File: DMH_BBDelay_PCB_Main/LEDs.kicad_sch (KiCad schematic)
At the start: 19 parts, among them Q15 BC548, Q16 BC548, Q17 BC548, Q18 BC548, SW2 SW_DPDT_x2, U19 4020, U20 4020

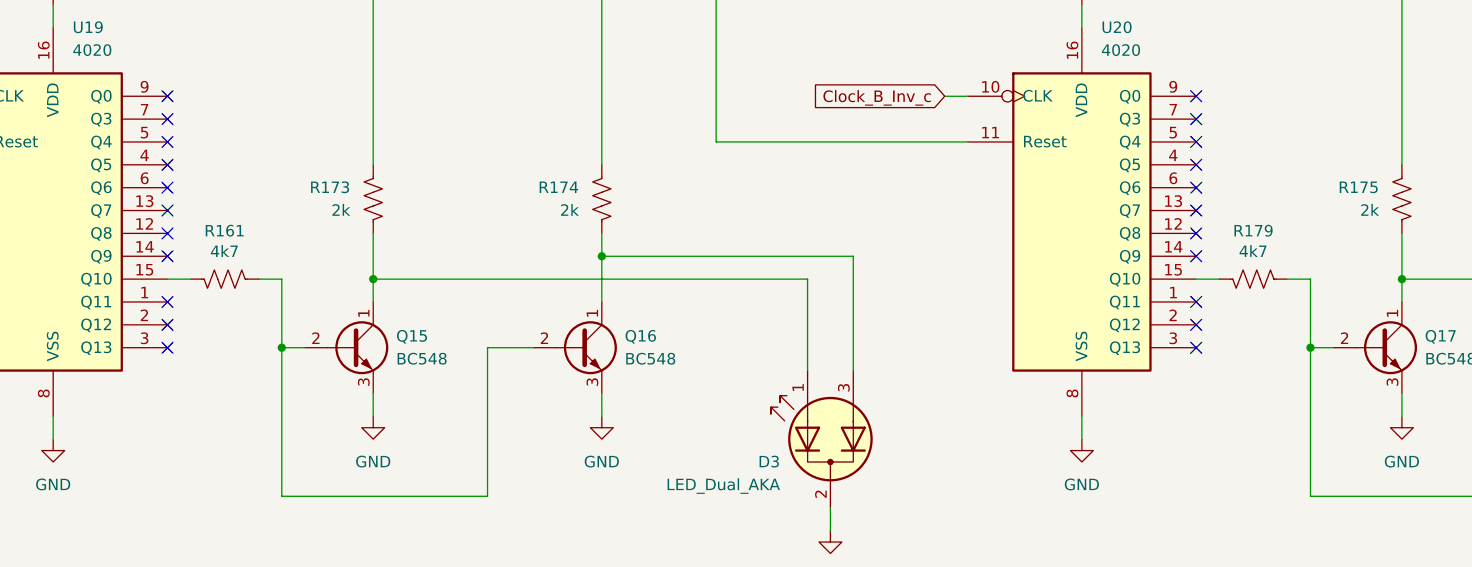
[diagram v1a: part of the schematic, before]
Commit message: Perfected circuit with double V3205
Next step is try quad V3205 per channel to reduce aliasing further
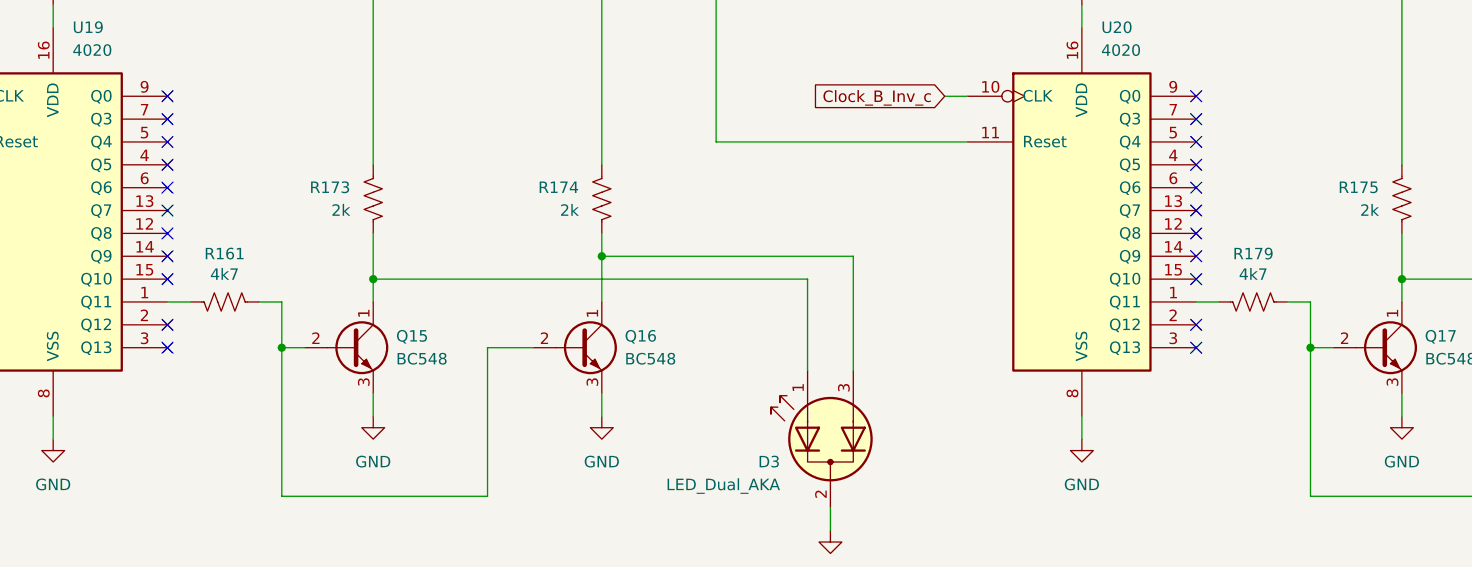
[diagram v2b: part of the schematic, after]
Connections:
- net at U19.1 (Q11): now also R161.1
- net at U19.15 (Q10): no longer R161.1
- net at R179.1: now also U20.1 (Q11); no longer U20.15 (Q10)
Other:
- moved on the sheet: R161, R179
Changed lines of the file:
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@@
 	)
 	(no_connect
-		(at 66.04 91.44)
+		(at 180.34 109.22)
 	)
 	(no_connect
-		(at 66.04 116.84)
+		(at 66.04 91.44)
 	)
 	(no_connect
-		(at 180.34 111.76)
+		(at 66.04 116.84)
 	)
 	(no_connect
@@
 	)
 	(no_connect
+		(at 66.04 109.22)
+	)
+	(no_connect
 		(at 180.34 106.68)
 	)
@@
 	)
 	(no_connect
-		(at 66.04 111.76)
-	)
-	(no_connect
 		(at 180.34 116.84)
 	)
@@
 	(wire
 		(pts
-			(xy 66.04 109.22) (xy 68.58 109.22)
+			(xy 127 69.85) (xy 38.1 69.85)
 		)
 		(stroke
@@
 	(wire
 		(pts
-			(xy 127 69.85) (xy 38.1 69.85)
+			(xy 78.74 111.76) (xy 76.2 111.76)
 		)
 		(stroke
@@
 	(wire
 		(pts
-			(xy 78.74 109.22) (xy 76.2 109.22)
+			(xy 114.3 66.04) (xy 142.24 66.04)
 		)
 		(stroke
@@
 	(wire
 		(pts
-			(xy 114.3 66.04) (xy 142.24 66.04)
+			(xy 180.34 111.76) (xy 182.88 111.76)
 		)
 		(stroke
@@
 	(wire
 		(pts
-			(xy 190.5 109.22) (xy 193.04 109.22)
+			(xy 190.5 111.76) (xy 193.04 111.76)
 		)
 		(stroke
@@
 	(wire
 		(pts
-			(xy 78.74 109.22) (xy 78.74 116.84)
+			(xy 78.74 111.76) (xy 78.74 116.84)
 		)
 		(stroke
@@
 	(wire
 		(pts
-			(xy 180.34 109.22) (xy 182.88 109.22)
-		)
-		(stroke
-			(width 0)
-			(type default)
-		)
-	)
-	(wire
-		(pts
 			(xy 38.1 93.98) (xy 38.1 69.85)
 		)
@@
 	(wire
 		(pts
-			(xy 193.04 109.22) (xy 193.04 116.84)
+			(xy 193.04 111.76) (xy 193.04 116.84)
+		)
+		(stroke
+			(width 0)
+			(type default)
+		)
+	)
+	(wire
+		(pts
+			(xy 66.04 111.76) (xy 68.58 111.76)
 		)
 		(stroke
@@
 	(symbol
 		(lib_id "Device:R_US")
-		(at 186.69 109.22 90)
+		(at 186.69 111.76 90)
 		(mirror x)
 		(unit 1)
@@
 		(dnp no)
 		(property "Reference" "R179"
-			(at 186.69 103.886 90)
+			(at 186.69 106.426 90)
 			(show_name no)
 			(do_not_autoplace no)
@@
 		)
 		(property "Value" "4k7"
-			(at 186.69 106.172 90)
+			(at 186.69 108.712 90)
 			(show_name no)
 			(do_not_autoplace no)
@@
 		)
 		(property "Footprint" "Resistor_THT:R_Axial_DIN0207_L6.3mm_D2.5mm_P7.62mm_Horizontal"
-			(at 186.944 110.236 90)
+			(at 186.944 112.776 90)
 			(hide yes)
 			(show_name no)
@@
 		)
 		(property "Datasheet" ""
-			(at 186.69 109.22 0)
+			(at 186.69 111.76 0)
 			(hide yes)
 			(show_name no)
@@
 		)
 		(property "Description" "Resistor, US symbol"
-			(at 186.69 109.22 0)
+			(at 186.69 111.76 0)
 			(hide yes)
 			(show_name no)
@@
 	(symbol
 		(lib_id "Device:R_US")
-		(at 72.39 109.22 90)
+		(at 72.39 111.76 90)
 		(mirror x)
 		(unit 1)
@@
 		(dnp no)
 		(property "Reference" "R161"
-			(at 72.39 103.886 90)
+			(at 72.39 106.426 90)
 			(show_name no)
 			(do_not_autoplace no)
@@
 		)
 		(property "Value" "4k7"
-			(at 72.39 106.172 90)
+			(at 72.39 108.712 90)
 			(show_name no)
 			(do_not_autoplace no)
@@
 		)
 		(property "Footprint" "Resistor_THT:R_Axial_DIN0207_L6.3mm_D2.5mm_P7.62mm_Horizontal"
-			(at 72.644 110.236 90)
+			(at 72.644 112.776 90)
 			(hide yes)
 			(show_name no)
@@
 		)
 		(property "Datasheet" ""
-			(at 72.39 109.22 0)
+			(at 72.39 111.76 0)
 			(hide yes)
 			(show_name no)
@@
 		)
 		(property "Description" "Resistor, US symbol"
-			(at 72.39 109.22 0)
+			(at 72.39 111.76 0)
 			(hide yes)
 			(show_name no)

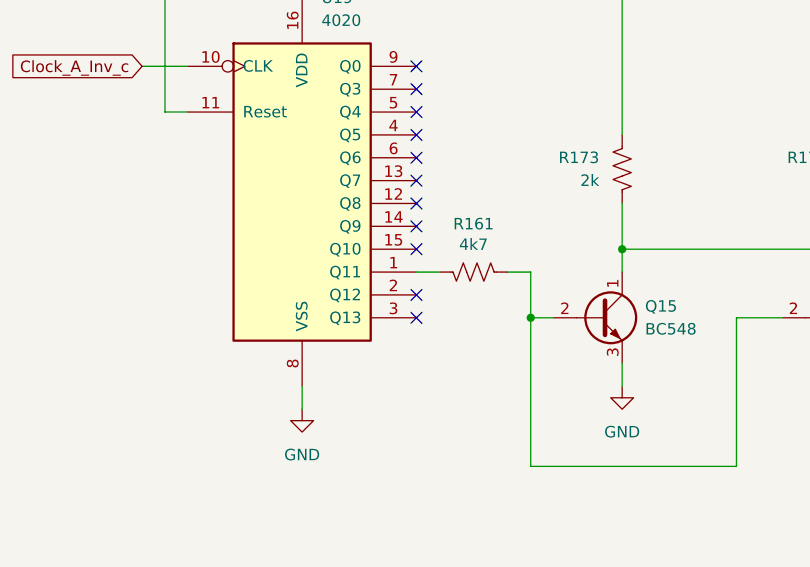
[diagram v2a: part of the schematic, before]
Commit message: Found RC network to scale and offset V3205 output
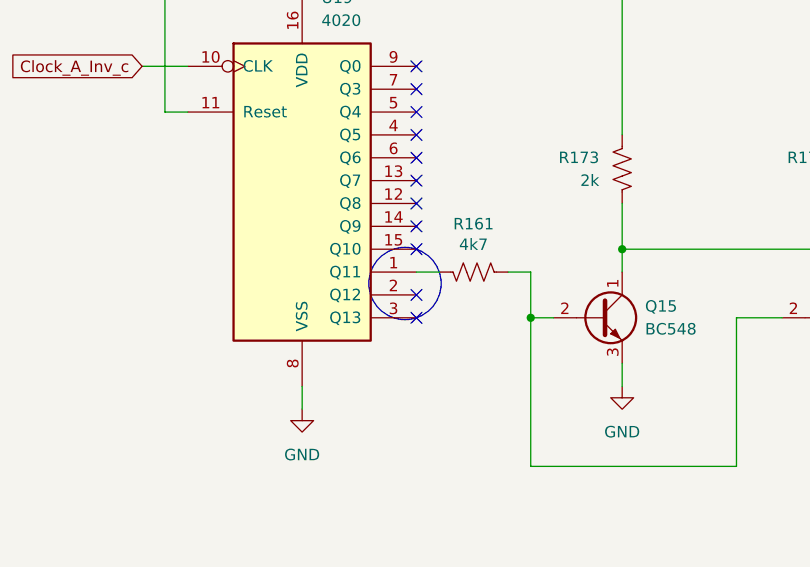
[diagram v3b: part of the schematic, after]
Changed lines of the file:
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@@
 		(comment 1 "PCB for 10cm Kosmo format synthesizer module")
+	)
+	(circle
+		(center 64.77 113.03)
+		(radius 4.0161)
+		(stroke
+			(width 0)
+			(type default)
+		)
+		(fill
+			(type none)
+		)
 	)
 	(rectangle

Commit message: Qualified channel A on breadboard
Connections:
- net at U19.1 (Q11): no longer R161.1
- net at U19.2 (Q12): now also R161.1
- net at R179.1: now also U20.2 (Q12); no longer U20.1 (Q11)
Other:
- moved on the sheet: R161, R179
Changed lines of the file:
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@@
 		(comment 1 "PCB for 10cm Kosmo format synthesizer module")
 	)
-	(circle
-		(center 64.77 113.03)
-		(radius 4.0161)
-		(stroke
-			(width 0)
-			(type default)
-		)
-		(fill
-			(type none)
-		)
-	)
 	(rectangle
 		(start 19.05 19.05)
@@
 	)
 	(no_connect
+		(at 180.34 111.76)
+	)
+	(no_connect
 		(at 66.04 101.6)
 	)
@@
 	)
 	(no_connect
-		(at 66.04 114.3)
-	)
-	(no_connect
 		(at 180.34 93.98)
 	)
@@
 	)
 	(no_connect
-		(at 180.34 114.3)
-	)
-	(no_connect
-		(at 180.34 116.84)
+		(at 66.04 111.76)
 	)
 	(no_connect
@@
 		(at 180.34 88.9)
 	)
+	(no_connect
+		(at 180.34 116.84)
+	)
 	(wire
 		(pts
@@
 	(wire
 		(pts
-			(xy 78.74 111.76) (xy 76.2 111.76)
+			(xy 78.74 114.3) (xy 76.2 114.3)
 		)
 		(stroke
@@
 	(wire
 		(pts
-			(xy 180.34 111.76) (xy 182.88 111.76)
-		)
-		(stroke
-			(width 0)
-			(type default)
-		)
-	)
-	(wire
-		(pts
 			(xy 88.9 121.92) (xy 88.9 124.46)
 		)
@@
 	(wire
 		(pts
+			(xy 66.04 114.3) (xy 68.58 114.3)
+		)
+		(stroke
+			(width 0)
+			(type default)
+		)
+	)
+	(wire
+		(pts
 			(xy 137.16 60.96) (xy 88.9 60.96)
 		)
@@
 	(wire
 		(pts
-			(xy 190.5 111.76) (xy 193.04 111.76)
+			(xy 190.5 114.3) (xy 193.04 114.3)
 		)
 		(stroke
@@
 	(wire
 		(pts
-			(xy 78.74 111.76) (xy 78.74 116.84)
+			(xy 78.74 114.3) (xy 78.74 116.84)
 		)
 		(stroke
@@
 	(wire
 		(pts
-			(xy 203.2 121.92) (xy 203.2 124.46)
+			(xy 180.34 114.3) (xy 182.88 114.3)
 		)
 		(stroke
@@
 	(wire
 		(pts
-			(xy 228.6 121.92) (xy 228.6 124.46)
+			(xy 203.2 121.92) (xy 203.2 124.46)
 		)
 		(stroke
@@
 	(wire
 		(pts
-			(xy 88.9 60.96) (xy 88.9 96.52)
+			(xy 228.6 121.92) (xy 228.6 124.46)
 		)
 		(stroke
@@
 	(wire
 		(pts
-			(xy 88.9 104.14) (xy 88.9 109.22)
+			(xy 88.9 60.96) (xy 88.9 96.52)
 		)
 		(stroke
@@
 	(wire
 		(pts
-			(xy 127 93.98) (xy 127 69.85)
+			(xy 88.9 104.14) (xy 88.9 109.22)
 		)
 		(stroke
@@
 	(wire
 		(pts
-			(xy 193.04 111.76) (xy 193.04 116.84)
+			(xy 127 93.98) (xy 127 69.85)
 		)
 		(stroke
@@
 	(wire
 		(pts
-			(xy 66.04 111.76) (xy 68.58 111.76)
+			(xy 193.04 114.3) (xy 193.04 116.84)
 		)
 		(stroke
@@
 	(symbol
 		(lib_id "Device:R_US")
-		(at 186.69 111.76 90)
+		(at 186.69 114.3 90)
 		(mirror x)
 		(unit 1)
@@
 		(dnp no)
 		(property "Reference" "R179"
-			(at 186.69 106.426 90)
+			(at 186.69 108.966 90)
 			(show_name no)
 			(do_not_autoplace no)
@@
 		)
 		(property "Value" "4k7"
-			(at 186.69 108.712 90)
+			(at 186.69 111.252 90)
 			(show_name no)
 			(do_not_autoplace no)
@@
 		)
 		(property "Footprint" "Resistor_THT:R_Axial_DIN0207_L6.3mm_D2.5mm_P7.62mm_Horizontal"
-			(at 186.944 112.776 90)
+			(at 186.944 115.316 90)
 			(hide yes)
 			(show_name no)
@@
 		)
 		(property "Datasheet" ""
-			(at 186.69 111.76 0)
+			(at 186.69 114.3 0)
 			(hide yes)
 			(show_name no)
@@
 		)
 		(property "Description" "Resistor, US symbol"
-			(at 186.69 111.76 0)
+			(at 186.69 114.3 0)
 			(hide yes)
 			(show_name no)
@@
 	(symbol
 		(lib_id "Device:R_US")
-		(at 72.39 111.76 90)
+		(at 72.39 114.3 90)
 		(mirror x)
 		(unit 1)
@@
 		(dnp no)
 		(property "Reference" "R161"
-			(at 72.39 106.426 90)
+			(at 72.39 108.966 90)
 			(show_name no)
 			(do_not_autoplace no)
@@
 		)
 		(property "Value" "4k7"
-			(at 72.39 108.712 90)
+			(at 72.39 111.252 90)
 			(show_name no)
 			(do_not_autoplace no)
@@
 		)
 		(property "Footprint" "Resistor_THT:R_Axial_DIN0207_L6.3mm_D2.5mm_P7.62mm_Horizontal"
-			(at 72.644 112.776 90)
+			(at 72.644 115.316 90)
 			(hide yes)
 			(show_name no)
@@
 		)
 		(property "Datasheet" ""
-			(at 72.39 111.76 0)
+			(at 72.39 114.3 0)
 			(hide yes)
 			(show_name no)
@@
 		)
 		(property "Description" "Resistor, US symbol"
-			(at 72.39 111.76 0)
+			(at 72.39 114.3 0)
 			(hide yes)
 			(show_name no)
